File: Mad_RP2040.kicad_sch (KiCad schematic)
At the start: 28 parts, among them J1 USB_C_Receptacle, SW1 SW_SPST, SW2 SW_SPST, T1 Tab, T2 Tab, T3 Tab, T4 Tab, U0 PCB, U1 ECMF02-2AMX6

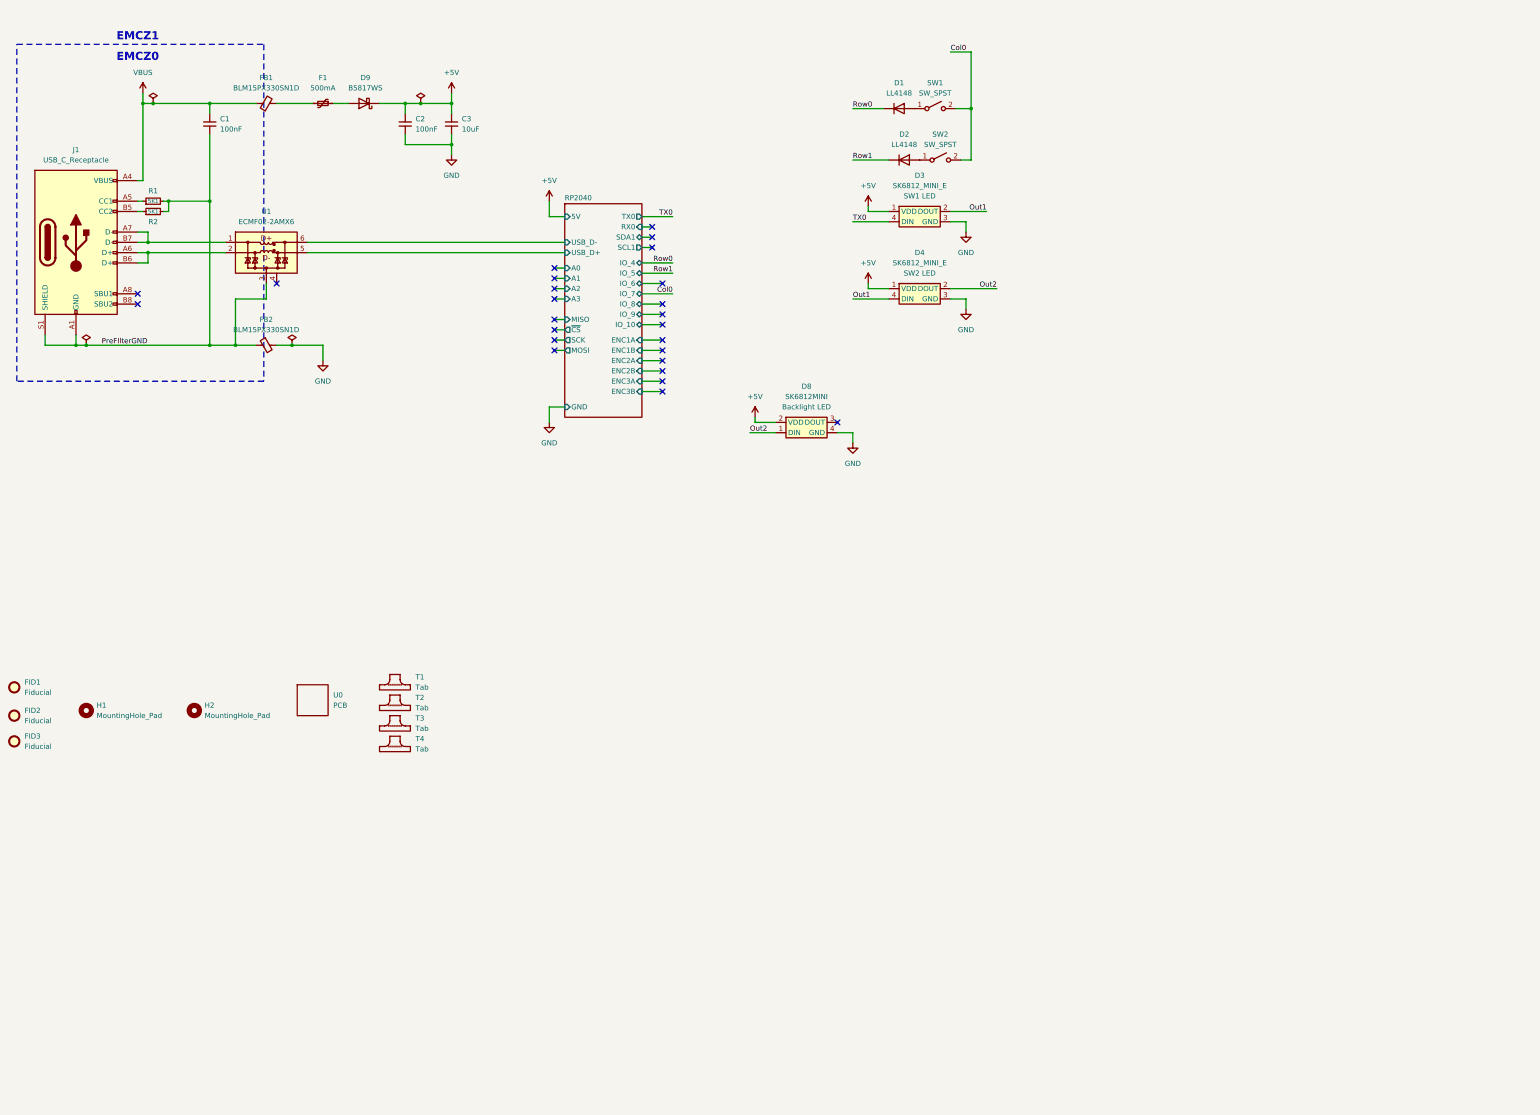
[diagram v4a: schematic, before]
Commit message: Expand board to 4x5, update rev to b
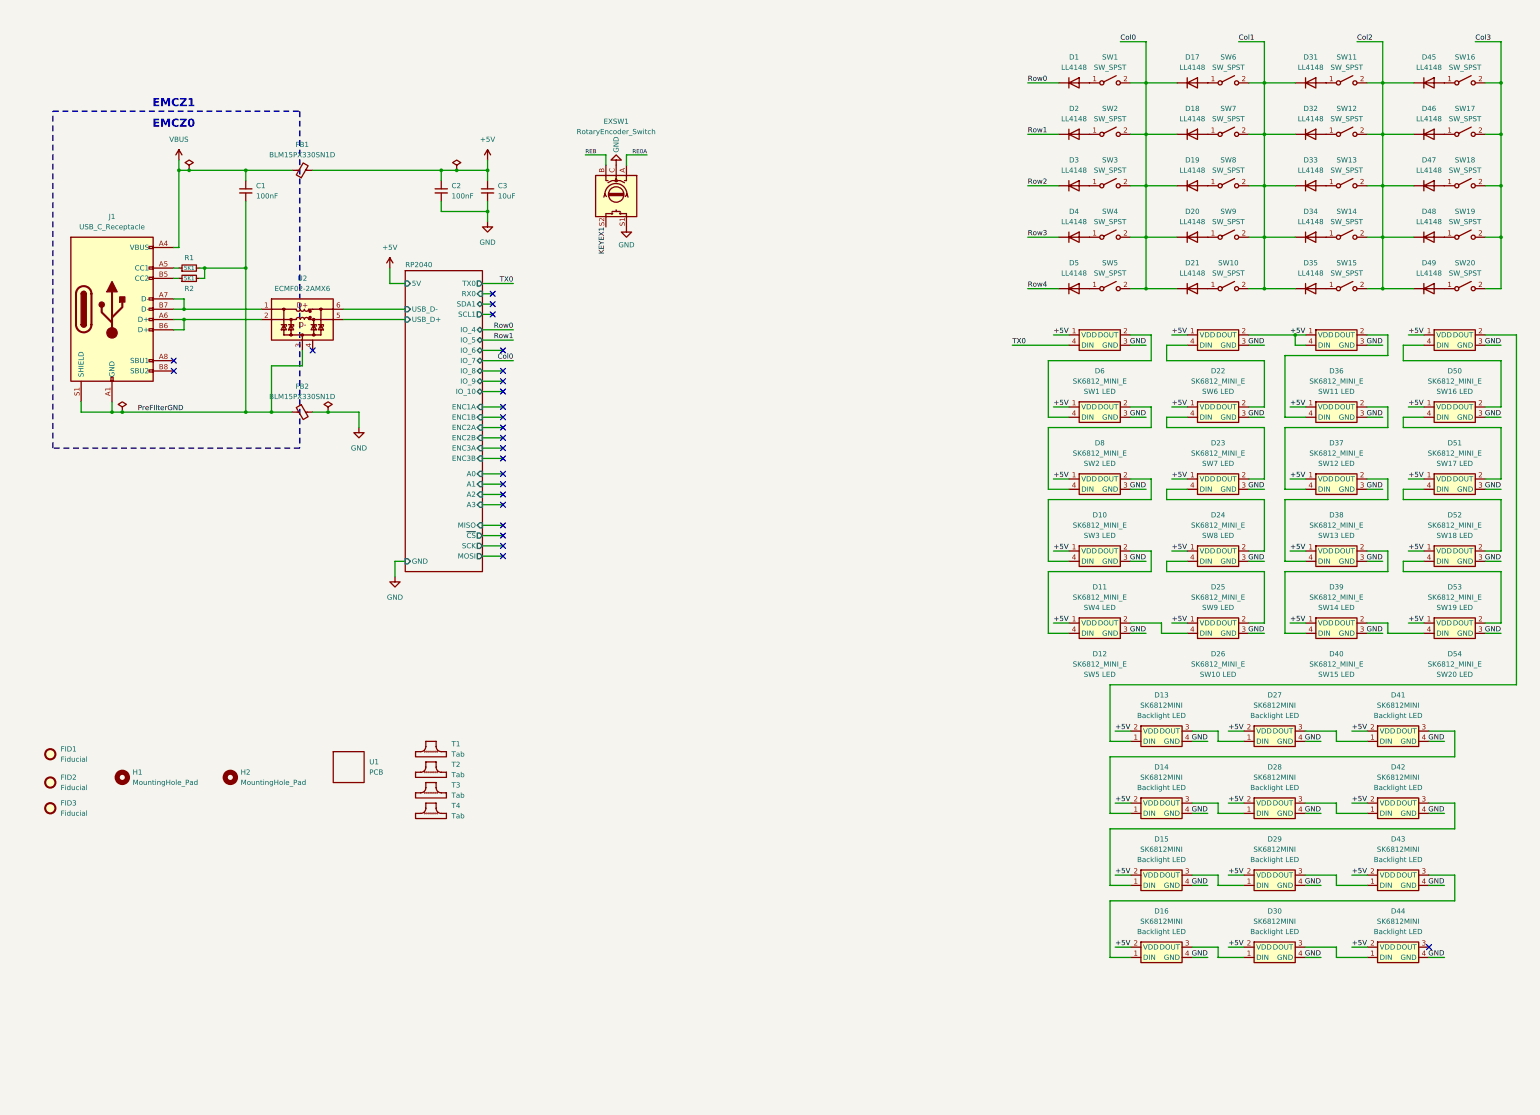
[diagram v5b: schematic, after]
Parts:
- removed D9: B5817WS, Diode_SMD:D_SOD-323, symbol Device:D_Schottky
- removed F1: 500mA, Fuse:Fuse_0402_1005Metric, symbol Device:Polyfuse_Small
- added D10, D11, D12, D22, D23, D24, D25, D26, D36, D37, D38, D39, D40, D50, D51, D52, D53, D54: SK6812_MINI_E, Mad_Footprints:SK6812MINI-E, symbol Mad_Symbols:SK6812MINI-E
- added D14, D15, D16, D27, D28, D29, D30, D41, D42, D43, D44: SK6812MINI, Mad_Footprints:SK6812MINI-012, symbol Mad_Symbols:SK6812MINI-012
- added D17, D18, D19, D20, D21, D3, D31, D32, D33, D34, D35, D4, D45, D46, D47, D48, D49, D5: LL4148, Diode_SMD:D_MiniMELF, symbol Diode:LL4148
- added EXSW1: RotaryEncoder_Switch, kbd_local:keyswitch_cherrymx_hotswap_1u_rotary_encoder_ec12, symbol Device:RotaryEncoder_Switch
- added SW10, SW11, SW12, SW13, SW14, SW15, SW16, SW17, SW18, SW19, SW20, SW3, SW4, SW5, SW6, SW7, SW8, SW9: SW_SPST, Mad_Footprints:SW_Hotswap_Kailh_MX_1.00u, symbol Switch:SW_SPST
- renumbered D8 to D13, D3 to D6, D4 to D8, U0 to U1, U1 to U2
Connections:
- net +5V: now also FB1.2, D10.1 (VDD), D11.1 (VDD), D12.1 (VDD), D14.2 (VDD), D15.2 (VDD), D16.2 (VDD), D22.1 (VDD), D22.2 (DOUT), D23.1 (VDD), D24.1 (VDD), D25.1 (VDD), D26.1 (VDD), D27.2 (VDD), D28.2 (VDD), D29.2 (VDD), D30.2 (VDD), D36.1 (VDD), D36.4 (DIN), D37.1 (VDD), D38.1 (VDD), D39.1 (VDD), D40.1 (VDD), D41.2 (VDD), D42.2 (VDD), D43.2 (VDD), D44.2 (VDD), D50.1 (VDD), D51.1 (VDD), D52.1 (VDD), D53.1 (VDD), D54.1 (VDD)
- net Col0: now also D17.1 (K), D18.1 (K), D19.1 (K), D20.1 (K), D21.1 (K), SW3.2 (B), SW4.2 (B), SW5.2 (B)
- net GND: now also D10.3 (GND), D11.3 (GND), D12.3 (GND), D14.4 (GND), D15.4 (GND), D16.4 (GND), D22.3 (GND), D23.3 (GND), D24.3 (GND), D25.3 (GND), D26.3 (GND), D27.4 (GND), D28.4 (GND), D29.4 (GND), D30.4 (GND), D36.3 (GND), D37.3 (GND), D38.3 (GND), D39.3 (GND), D40.3 (GND), D41.4 (GND), D42.4 (GND), D43.4 (GND), D44.4 (GND), D50.3 (GND), D51.3 (GND), D52.3 (GND), D53.3 (GND), D54.3 (GND), EXSW1.C, EXSW1.S1
- net at D13.3 (DOUT): now also D27.1 (DIN)
- net Out1: no longer names the net of D6.2 (DOUT), D8.4 (DIN)
- net Out2: no longer names the net of D13.1 (DIN)
- net Out2: now also D50.2 (DOUT); no longer D8.2 (DOUT)
- new net: D14.1 (DIN), D41.3 (DOUT)
- new net: D14.3 (DOUT), D28.1 (DIN)
- new net: D34.2 (A), SW14.1 (A)
- new net: D30.3 (DOUT), D44.1 (DIN)
- new net: D10.2 (DOUT), D11.4 (DIN)
- new net: D10.4 (DIN), D8.2 (DOUT)
- new net: D46.2 (A), SW17.1 (A)
- new net: D50.4 (DIN), D51.2 (DOUT)
- new net: D31.2 (A), SW11.1 (A)
- new net: D33.2 (A), SW13.1 (A)
- new net: D32.2 (A), SW12.1 (A)
- new net: D39.2 (DOUT), D40.4 (DIN)
- new net: D38.2 (DOUT), D39.4 (DIN)
- new net: D51.4 (DIN), D52.2 (DOUT)
- new net: D52.4 (DIN), D53.2 (DOUT)
- new net: D47.2 (A), SW18.1 (A)
- new net: D48.2 (A), SW19.1 (A)
- new net: D15.1 (DIN), D42.3 (DOUT)
- new net: D15.3 (DOUT), D29.1 (DIN)
- new net: D17.2 (A), SW6.1 (A)
- new net: D21.2 (A), SW10.1 (A)
- new net: D29.3 (DOUT), D43.1 (DIN)
- new net: D16.1 (DIN), D43.3 (DOUT)
- new net: D4.2 (A), SW4.1 (A)
- new net: D20.2 (A), SW9.1 (A)
- new net: D49.2 (A), SW20.1 (A)
- new net: D3.2 (A), SW3.1 (A)
- new net: D25.4 (DIN), D26.2 (DOUT)
- new net: D12.2 (DOUT), D26.4 (DIN)
- new net: D23.4 (DIN), D24.2 (DOUT)
- new net: D24.4 (DIN), D25.2 (DOUT)
- new net: D5.2 (A), SW5.1 (A)
- new net: D40.2 (DOUT), D54.4 (DIN)
- new net: D35.2 (A), SW15.1 (A)
- new net: D36.2 (DOUT), D37.4 (DIN)
- new net: D53.4 (DIN), D54.2 (DOUT)
- new net: D11.2 (DOUT), D12.4 (DIN)
- new net: D16.3 (DOUT), D30.1 (DIN)
- new net: D45.2 (A), SW16.1 (A)
- new net: D28.3 (DOUT), D42.1 (DIN)
- new net: D37.2 (DOUT), D38.4 (DIN)
- new net: D27.3 (DOUT), D41.1 (DIN)
- new net: D18.2 (A), SW7.1 (A)
- new net: D22.4 (DIN), D23.2 (DOUT)
- new net: D19.2 (A), SW8.1 (A)
- new net Col1: D31.1 (K), D32.1 (K), D33.1 (K), D34.1 (K), D35.1 (K), SW10.2 (B), SW6.2 (B), SW7.2 (B), SW8.2 (B), SW9.2 (B)
- new net Col2: D45.1 (K), D46.1 (K), D47.1 (K), D48.1 (K), D49.1 (K), SW11.2 (B), SW12.2 (B), SW13.2 (B), SW14.2 (B), SW15.2 (B)
- new net Col3: SW16.2 (B), SW17.2 (B), SW18.2 (B), SW19.2 (B), SW20.2 (B)
- new net KEYEX1: EXSW1.S2
- new net RE0A: EXSW1.A
- new net REB: EXSW1.B
- new net Row2: D3.1 (K)
- new net Row3: D4.1 (K)
- new net Row4: D5.1 (K)
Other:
- moved on the sheet: C1, C2, C3, D1, D13, D2, D6, D8, FB1, FB2, FID1, FID2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

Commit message: Rough placement of components. Remove one layer of keys (4x4 -> 4x3)
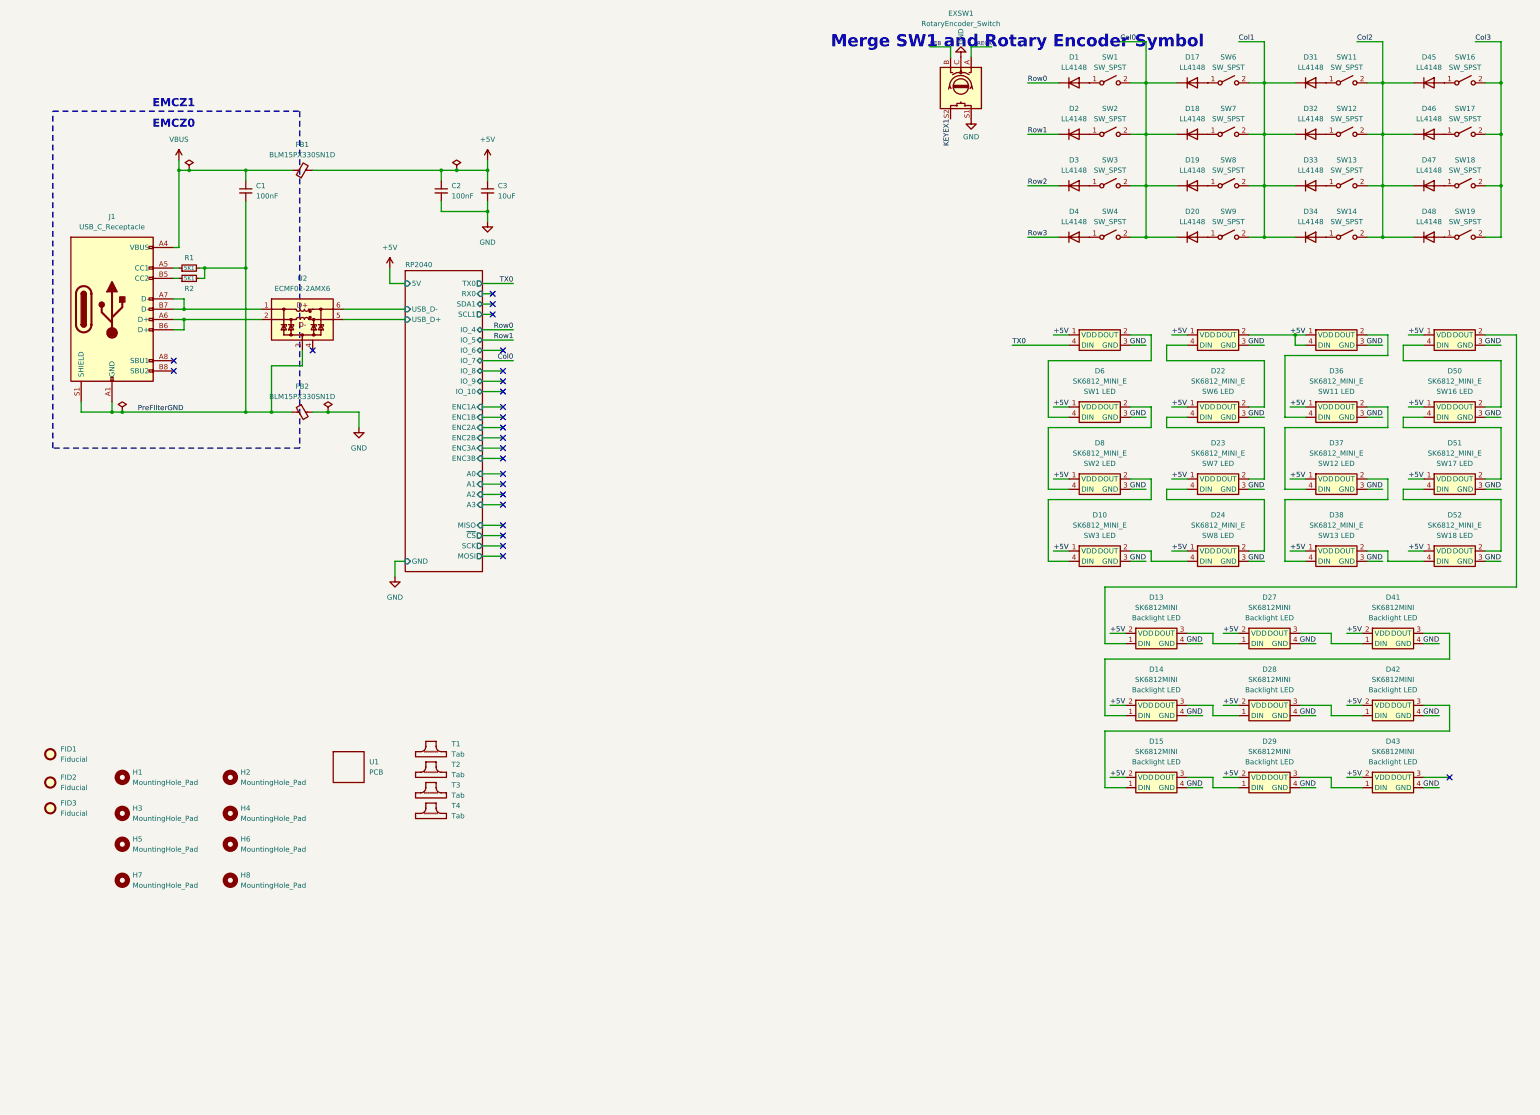
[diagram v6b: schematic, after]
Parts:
- removed D12, D26, D40, D54: SK6812_MINI_E, Mad_Footprints:SK6812MINI-E, symbol Mad_Symbols:SK6812MINI-E
- removed D16, D30, D44: SK6812MINI, Mad_Footprints:SK6812MINI-012, symbol Mad_Symbols:SK6812MINI-012
- removed D21, D35, D49, D5: LL4148, Diode_SMD:D_MiniMELF, symbol Diode:LL4148
- removed SW10, SW15, SW20, SW5: SW_SPST, Mad_Footprints:SW_Hotswap_Kailh_MX_1.00u, symbol Switch:SW_SPST
- added H3, H4, H5, H6, H7, H8: MountingHole_Pad, MountingHole:MountingHole_2.2mm_M2_DIN965, symbol Mechanical:MountingHole
- EXSW1: footprint kbd_local:keyswitch_cherrymx_hotswap_1u_rotary_encoder_ec12 -> kbd:keyswitch_choc12_hotswap_1u_rotary_encoder_ec12
- SW1: footprint Mad_Footprints:SW_Hotswap_Kailh_MX_1.00u -> kbd:keyswitch_choc12_hotswap_1u_rotary_encoder_ec12
- SW11, SW12, SW13, SW14, SW16, SW17, SW18, SW19, SW2, SW3, SW4, SW6, SW7, SW8, SW9: footprint Mad_Footprints:SW_Hotswap_Kailh_MX_1.00u -> kbd:keyswitch_choc12_hotswap_1u
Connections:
- net at D39.2 (DOUT): now also D53.4 (DIN)
- net at D25.4 (DIN): now also D11.2 (DOUT)
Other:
- note added: "Merge SW1 and Rotary Encoder Symbol"
- moved on the sheet: D13, D14, D15, D27, D28, D29, D41, D42, D43, EXSW1

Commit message: More placement, start routing, fix up some schematic connections
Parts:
- removed D14, D27, D28, D29, D42: SK6812MINI, Mad_Footprints:SK6812MINI-012, symbol Mad_Symbols:SK6812MINI-012
- removed H1, H3, H5, H7: MountingHole_Pad, MountingHole:MountingHole_2.2mm_M2_DIN965, symbol Mechanical:MountingHole
- removed SW1: SW_SPST, kbd:keyswitch_choc12_hotswap_1u_rotary_encoder_ec12, symbol Switch:SW_SPST
- added C23: 100nF, Capacitor_SMD:C_0402_1005Metric, symbol Device:C_Small
- added D16: SK6812MINI, Mad_Footprints:SK6812MINI-012, symbol Mad_Symbols:SK6812MINI-012
- added H10, H11: MountingHole_Pad, MountingHole:MountingHole_2.2mm_M2_DIN965, symbol Mechanical:MountingHole
- SW1: renamed from EXSW1; Config (none) -> -LCSC_BOM
- SW11, SW12, SW13, SW14, SW16, SW17, SW18, SW19, SW2, SW3, SW4, SW6, SW7, SW8, SW9: Config (none) -> -LCSC_BOM
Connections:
- net KEYEX1 is gone; now on net Col0: SW1.S2
- net +5V: now also D16.2 (VDD); no longer D22.2 (DOUT), D36.4 (DIN)
- net GND: now also D16.4 (GND); no longer SW1.S1
- net PreFIlterGND: now also C23.2
- net VBUS: now also C23.1
- net at D41.3 (DOUT): now also D16.1 (DIN)
- net at D13.3 (DOUT): now also D41.1 (DIN)
- net at D1.2 (A): now also SW1.S1
- net at D15.1 (DIN): now also D16.3 (DOUT)
- net at D15.3 (DOUT): now also D43.1 (DIN)
- net RE0A renamed REA
- new net: D22.2 (DOUT), D36.4 (DIN)
- no-connect marks 25 -> 18
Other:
- sheet RP2040 ports: added IO_11, IO_12; removed ENC3A, ENC3B
- note removed: "Merge SW1 and Rotary Encoder Symbol"
- moved on the sheet: C1, D1, D10, D13, D15, D17, D18, D19, D2, D20, D22, D23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
